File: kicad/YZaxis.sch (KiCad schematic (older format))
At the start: 31 parts, among them CON16 Stepstick_Left_Connector, CON17 Stepstick_Right_Connector, CON18 Stepstick_Left_Connector, CON19 Stepstick_Right_Connector, CON20 YZ, Q3 IRLR2905ZPBF, U1 CD4504BPW

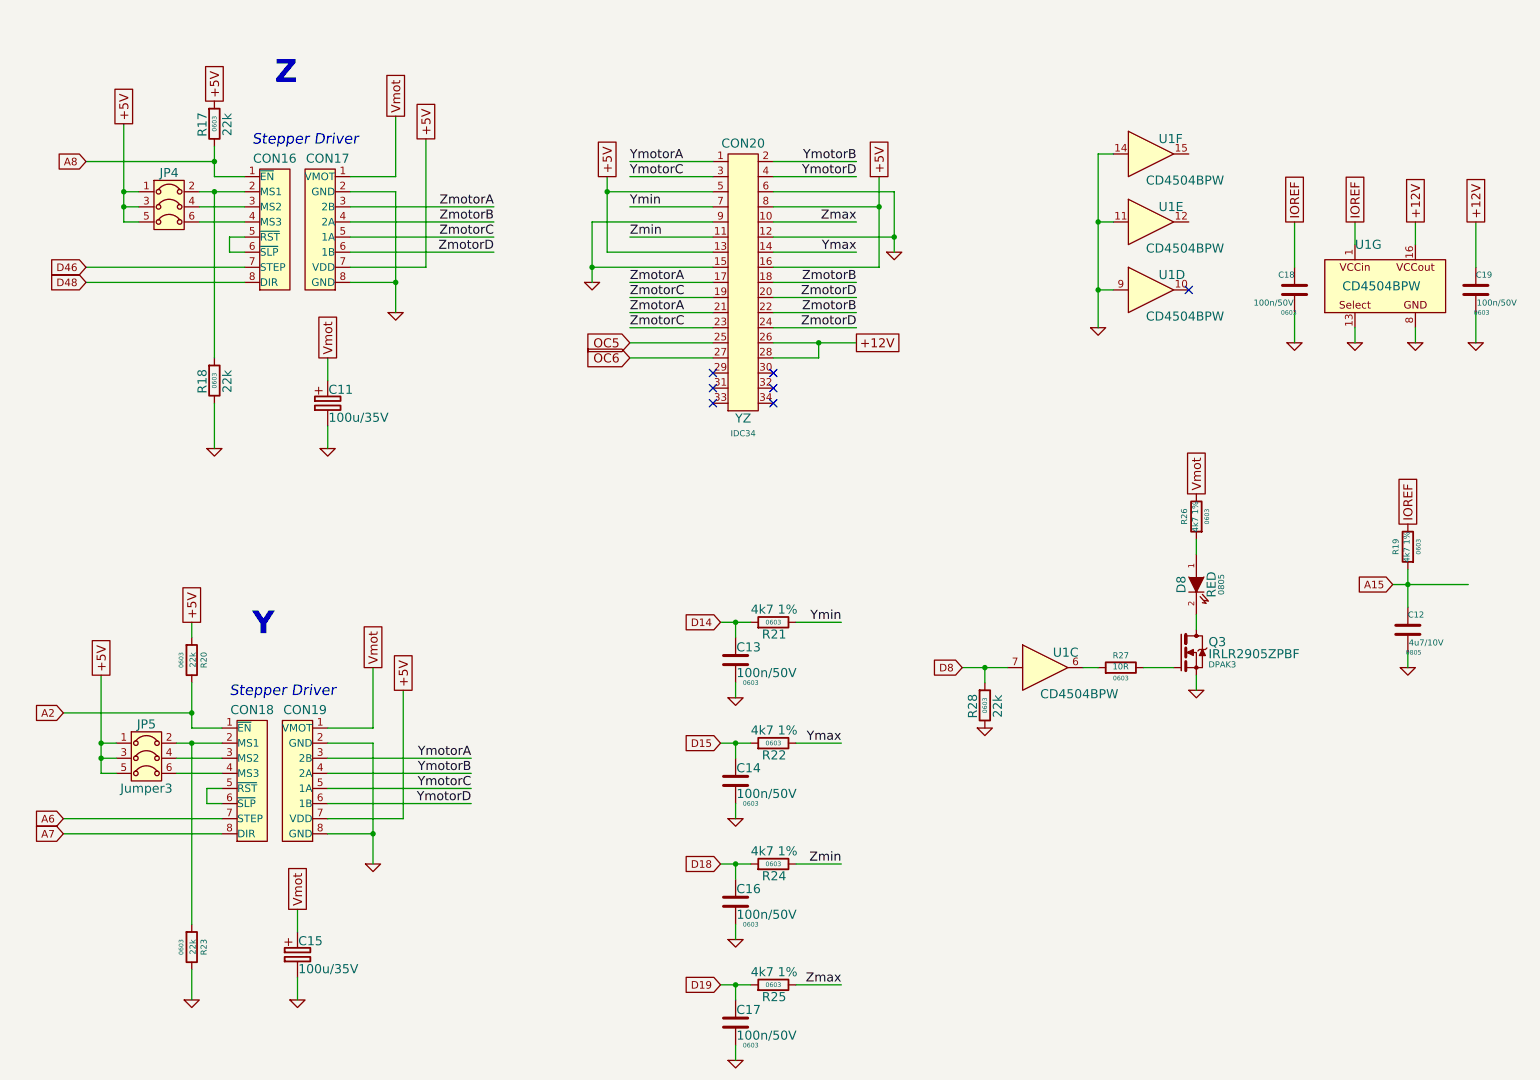
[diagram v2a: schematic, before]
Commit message: Change ULN2803 to discrete MOSFET's FDC6401N
Close #7
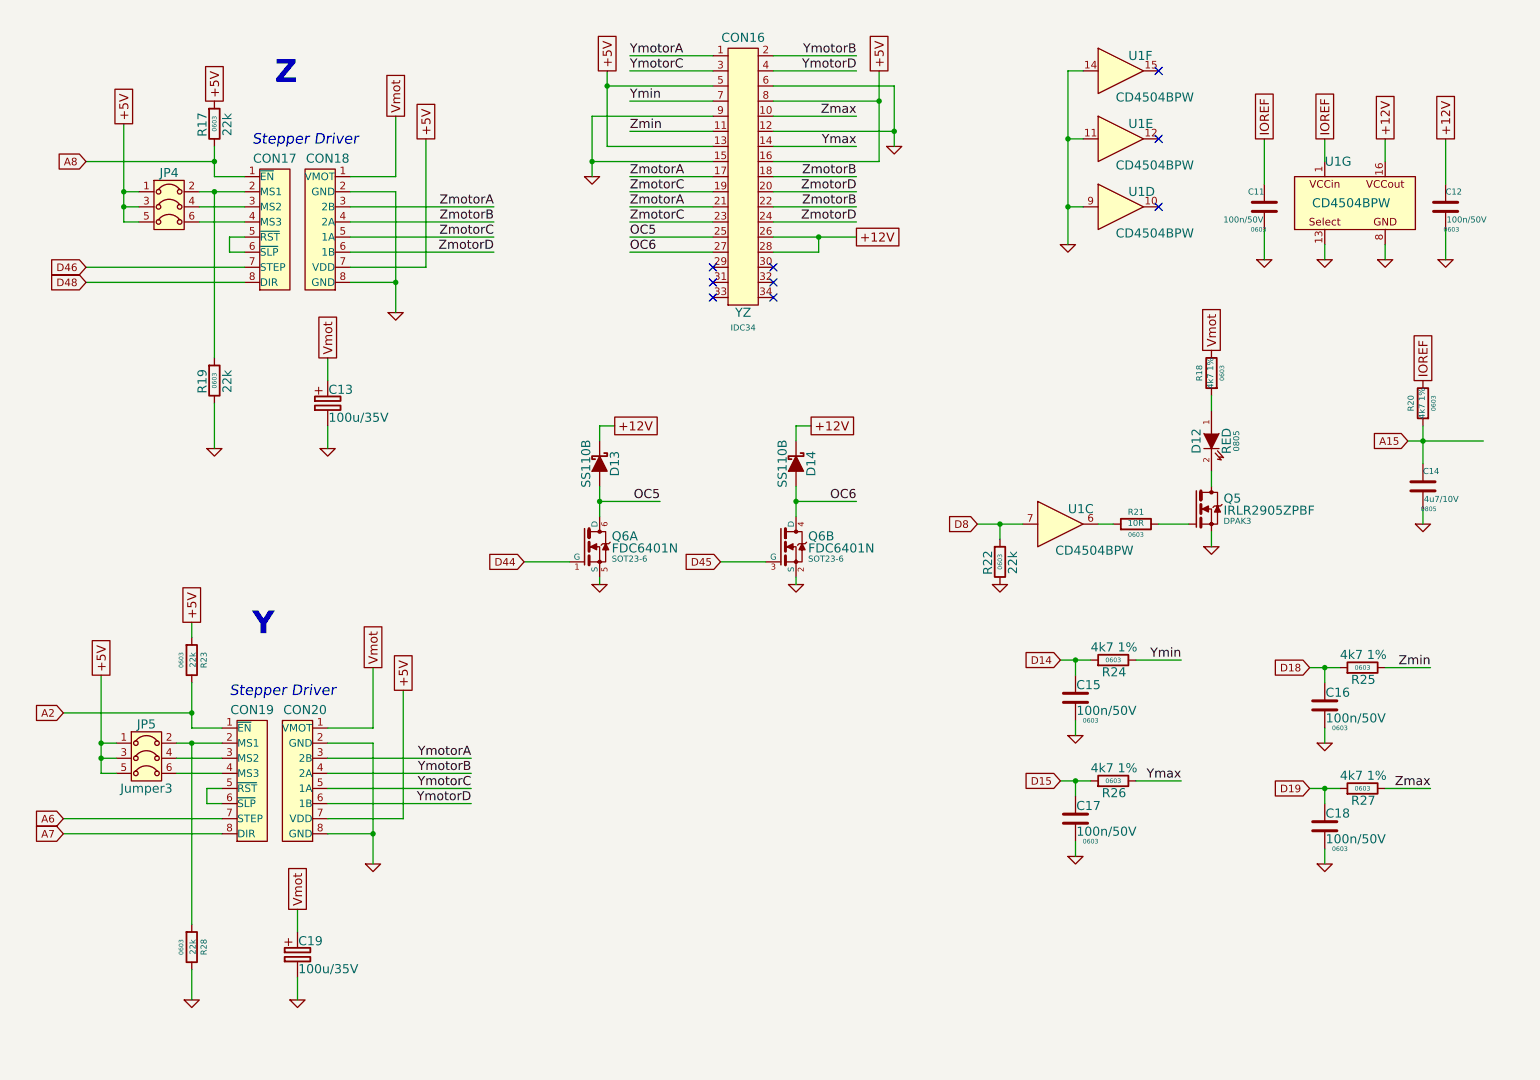
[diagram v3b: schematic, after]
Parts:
- added D13, D14: SS110B, symbol SS110B
- added Q6: FDC6401N, SOT23-6, symbol FDC6401N
- renumbered C18 to C11, C19 to C12, C11 to C13, C12 to C14, C13 to C15, C14 to C17, C17 to C18, C15 to C19, CON20 to CON16, CON16 to CON17, CON17 to CON18, CON18 to CON19, CON19 to CON20, D8 to D12, Q3 to Q5, R26 to R18, R18 to R19, R19 to R20, R27 to R21, R28 to R22, R20 to R23, R21 to R24, R24 to R25, R22 to R26, R25 to R27, R23 to R28
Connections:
- net +12V: now also D13.1, D14.1
- net GND: now also Q6.2 (S), Q6.5 (S)
- net OC5: now also D13.2, Q6.6 (D)
- net OC6: now also D14.2, Q6.4 (D)
- new net D44: Q6.1 (G)
- new net D45: Q6.3 (G)
- no-connect marks 7 -> 9
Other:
- moved on the sheet: C11, C12, C14, C15, C16, C17, C18, CON16, D12, Q5, R18, R20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

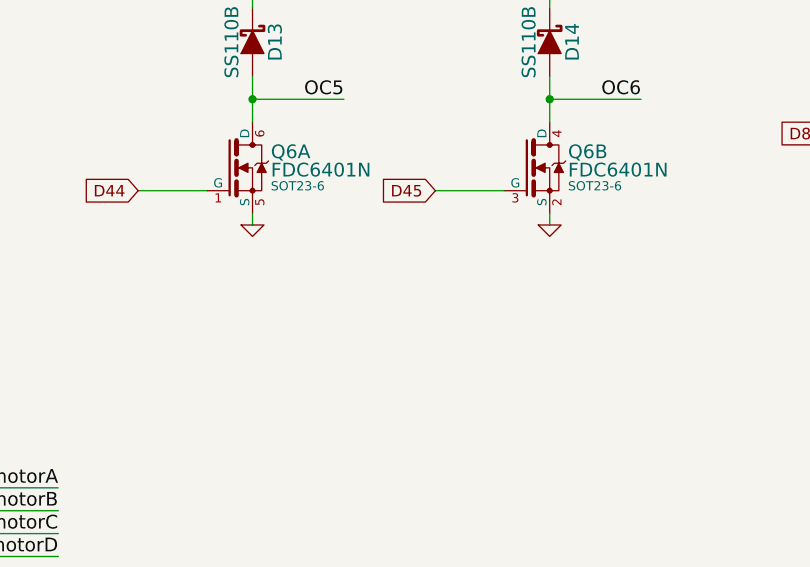
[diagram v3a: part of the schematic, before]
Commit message: Extract power supply circuits to another sheet. Add power off circuit.
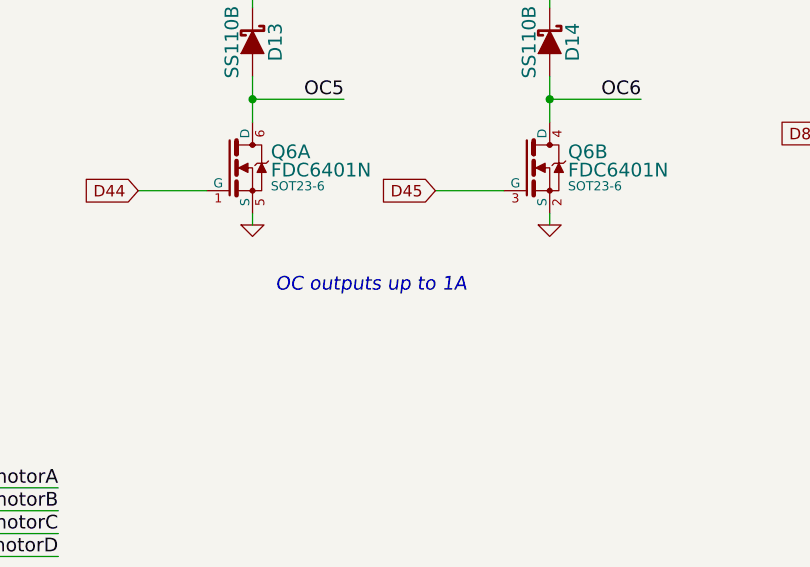
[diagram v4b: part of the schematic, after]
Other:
- note added: "OC outputs up to 1A"
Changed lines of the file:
@@
 $Descr A4 11693 8268
 encoding utf-8
-Sheet 3 4
+Sheet 3 5
 Title "Ramps plus"
 Date "16 apr 2014"
@@
 NoConn ~ 8400 1450
 NoConn ~ 8400 1000
+Text Notes 4800 4700 0    60   Italic 0
+OC outputs up to 1A
 $EndSCHEMATC
